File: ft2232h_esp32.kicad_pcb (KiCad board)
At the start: 4 copper layers, 21.8 x 49.3 mm, 70 parts, among them J1 USB_C_Receptacle_USB2.0, Q1 S8050, Q2 S8050, SW1 SW_SPDT, U1 ESP32FullConnector, U10 USBLC6-2SC6-Power_Protection, U11 USBLC6-2SC6-Power_Protection, U12 USBLC6-2SC6-Power_Protection, U13 USBLC6-2SC6-Power_Protection, U2 ESP32FullConnector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

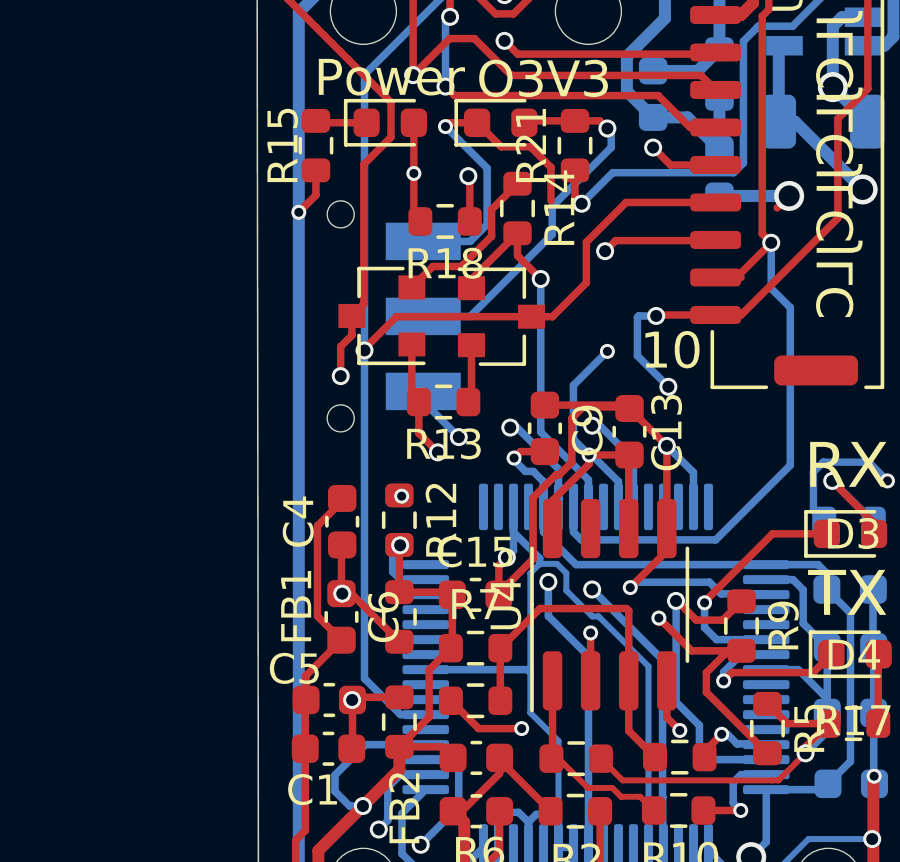
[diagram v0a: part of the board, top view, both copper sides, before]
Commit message: V4
Fix BJT bug
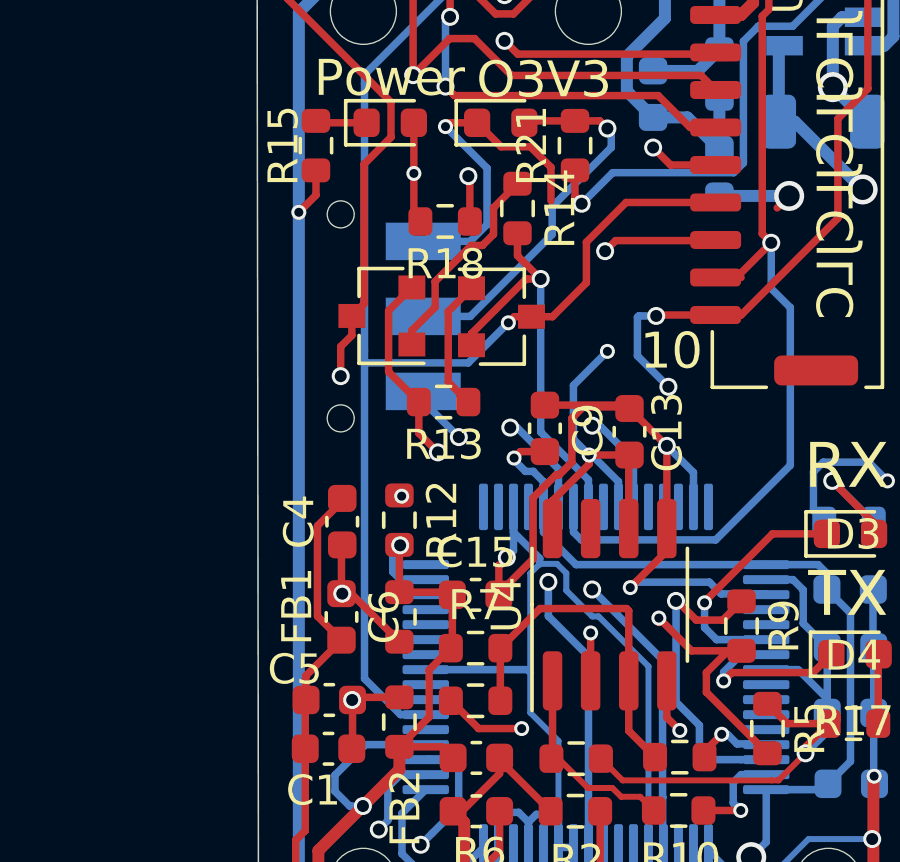
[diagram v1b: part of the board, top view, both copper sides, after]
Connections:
- Q1 pad 1: nRTS -> Net-(Q1-Pad1)
- Q1 pad 2: Net-(Q1-Pad2) -> nRTS
- Q2 pad 1: nDTR -> Net-(Q2-Pad1)
- Q2 pad 2: Net-(Q2-Pad2) -> nDTR
- R13 pad 1: Net-(Q1-Pad2) -> Net-(Q1-Pad1)
- R14 pad 1: Net-(Q2-Pad2) -> Net-(Q2-Pad1)
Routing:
- net Net-(Q2-Pad1): track 0.00 -> 7.03 mm
- net Net-(Q2-Pad2): track 5.47 -> 0.00 mm
- net Net-(Q1-Pad1): track 0.00 -> 4.39 mm
- net nDTR: track 13.5 -> 16.4 mm
- net Net-(Q1-Pad2): track 1.94 -> 0.00 mm
- net nRTS: track 12.6 -> 13.5 mm
